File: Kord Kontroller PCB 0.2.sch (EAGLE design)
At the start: 198 parts, among them J3 FTSH-105-01-L-DV-KJ, SW2 SPST_TACT-KMR2, U1 AP2112K-3.3, U2 ATSAMD51J19A-AUT, U3 SN74LV4T125PWR, Y1 ECS-.327-12.5-17X-TR

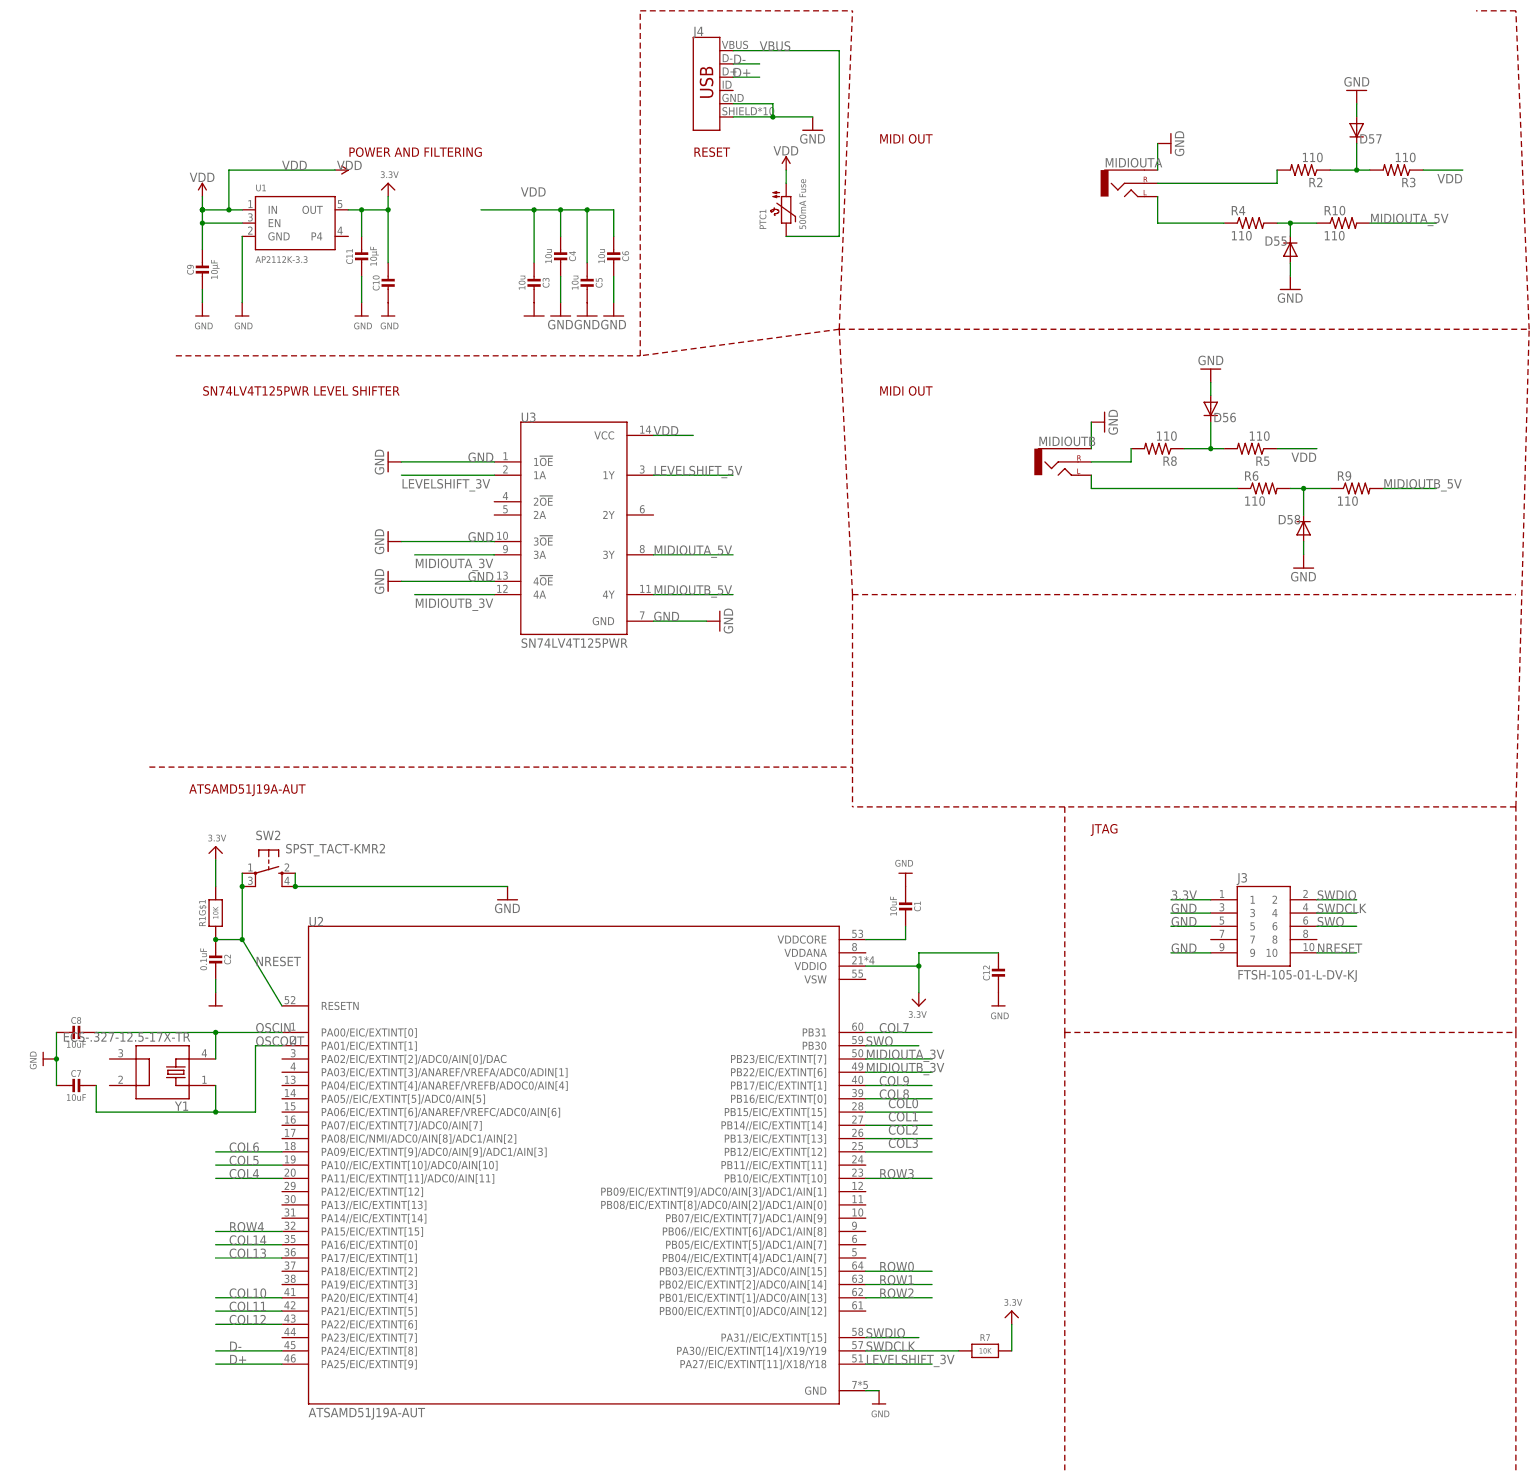
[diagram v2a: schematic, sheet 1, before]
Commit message: Added Capacitors for power management
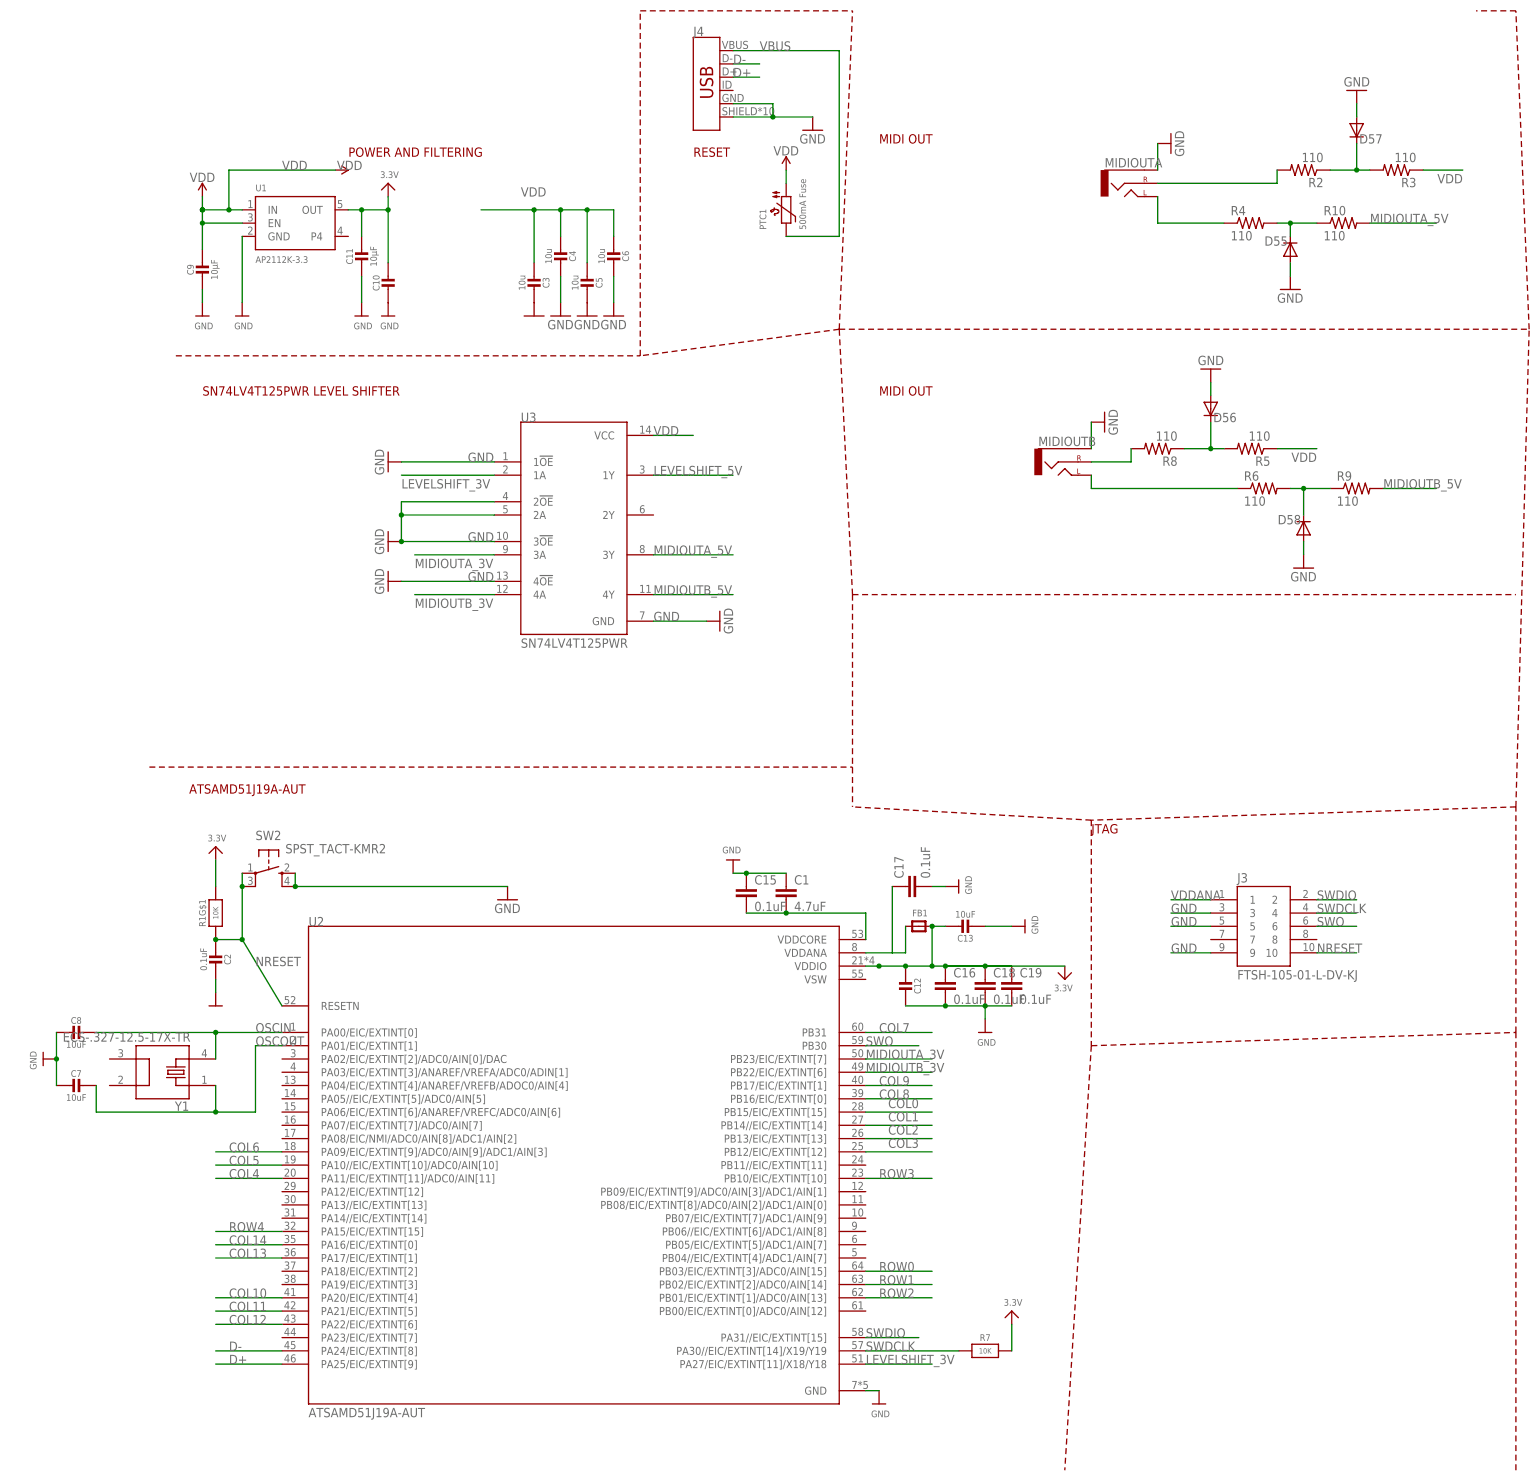
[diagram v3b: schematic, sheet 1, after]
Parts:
- added C13: 10uF, microbuilder:CAP_CERAMIC0805-NOOUTLINE
- added C15, C16, C17, C18, C19: 0.1uF, SparkFun-Capacitors:0.1UF-0603-25V-(+80/-20%)
- added FB1: (no value), microbuilder:FERRITE
- C1: value 10uF -> 4.7uF; device microbuilder:CAP_CERAMIC0805-NOOUTLINE -> SparkFun-Capacitors:4.7UF-0603-6.3V-(10%)
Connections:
- removed net 3.3V: C10.1, C11.1, C12.1, J3.1, R1G$1.2, R7.2, U1.OUT, U2.VDDIO
- new net N$74: C17.1, FB1.P$1, U2.VDDANA
- new net VDDANA: C10.1, C11.1, C12.2, C13.1, C16.1, C18.1, C19.1, FB1.P$2, J3.1, R1G$1.2, R7.2, U1.OUT, U2.VDDIO
- net GND: now also C1.1, C12.1, C13.2, C15.1, C16.2, C17.2, C18.2, C19.2, U3.2!OE, U3.2A; no longer C1.2, C12.2
- net VDDCORE1: now also C1.2, C15.2; no longer C1.1
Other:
- moved on the sheet: C1, C12

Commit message: REV-B
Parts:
- added TP1, TP10, TP12, TP13, TP14, TP15, TP16, TP17, TP18, TP19, TP2, TP20, TP21, TP22, TP23, TP24, TP25, TP26, TP27, TP28, TP29, TP3, TP30, TP31, TP32, TP33, TP34, TP35, TP36, TP37, TP5, TP6, TP7, TP8: (no value), microbuilder:TESTPOINTROUND1MM
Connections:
- removed net N$74: C17.1, FB1.P$1, U2.VDDANA
- new net VDDIO: C10.1, C11.1, C12.2, C13.1, C16.1, C18.1, C19.1, FB1.P$2, J3.1, R1G$1.2, R7.2, TP13.P$1, TP5.P$1, U1.OUT, U2.VDDIO
- net COL0: now also TP27.P$1
- net COL1: now also TP28.P$1
- net COL10: now also TP35.P$1
- net COL11: now also TP36.P$1
- net COL12: now also TP37.P$1
- net COL13: now also TP23.P$1
- net COL14: now also TP22.P$1
- net COL2: now also TP29.P$1
- net COL3: now also TP30.P$1
- net COL4: now also TP20.P$1
- net COL5: now also TP19.P$1
- net COL6: now also TP18.P$1
- net COL7: now also TP24.P$1
- net COL8: now also TP26.P$1
- net COL9: now also TP25.P$1
- net D+: now also TP3.P$1
- net D-: now also TP2.P$1
- net LEVELSHIFT_3V: now also TP6.P$1
- net MIDIOUTA_3V: now also TP7.P$1
- net MIDIOUTA_5V: now also TP12.P$1
- net MIDIOUTB_3V: now also TP8.P$1
- net MIDIOUTB_5V: now also TP10.P$1
- net NRESET: now also TP17.P$1
- net ROW0: now also TP32.P$1
- net ROW1: now also TP33.P$1
- net ROW2: now also TP34.P$1
- net ROW3: now also TP31.P$1
- net ROW4: now also TP21.P$1
- net SWDCLK: now also TP16.P$1
- net SWDIO: now also TP14.P$1
- net SWO: now also TP15.P$1
- net VBUS: now also TP1.P$1
- net VDDANA: now also C17.1, FB1.P$1, U2.VDDANA; no longer C10.1, C11.1, C12.2, C13.1, C16.1, C18.1, C19.1, FB1.P$2, J3.1, R1G$1.2, R7.2, U1.OUT, U2.VDDIO
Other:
- moved on the sheet: PTC1
